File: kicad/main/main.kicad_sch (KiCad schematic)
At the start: 52 parts, among them J1 to cam, J10 I2C_1, J11 drib-kick, J12 drib-kick, J14 5V OUT, J15 LINE, J3 USB_C_Receptacle_USB2.0, J4 Power IN, J5 MD1, J6 MD2, J7 Serial0/XBee, J8 Serial1/IMU, J9 AUX1, Q1 AO3400A, Q2 AO3401A, SW1 BTN_UP, SW2 BTN_UP, SW3 Reset, U2 RP2040_Stamp, U3 74HC32, U4 74HC04, U5 OKL-T_3-W12N-C

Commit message: main bus
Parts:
- J2: value (none) -> I2C_2; footprint (none) -> 0.main.robot:JSTB4B-ZR
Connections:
- net +5V: no longer J8.2 (Pin_2)
- net GND: now also SW?.1; no longer J8.4 (Pin_4)
- net SW1_5: no longer U2.8 (GPIO7)
- net IMU SET: now reaches SW?.2
- net IMU SET: now also U2.24 (GPIO23)
- net SCL_I2C0 renamed I2C_0.SCL
- net SCL_I2C1 renamed I2C_1.SCL
- net SDA_I2C0 renamed I2C_0.SDA
- net SDA_I2C1 renamed I2C_1.SDA
- net USB_D+ renamed USB.D+
- net USB_D- renamed USB.D-
- new net: J8.4 (Pin_4), U2.8 (GPIO7)
- no-connect marks 11 -> 14
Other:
- moved on the sheet: SW?

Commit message: update
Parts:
- gave numbers to parts that had none: 1
- renumbered C3 to C1, C4 to C2, C5 to C3, C6 to C4, D3 to D1, D4 to D2, D1 to D3, D5 to D4, D6 to D5, J3 to J1, J14 to J13, J15 to J14, J4 to J3, J5 to J4, J6 to J5, J7 to J6, J8 to J7, J9 to J8, J1 to J9, R3 to R1, R11 to R10, R12 to R11, R13 to R12, R14 to R13, R15 to R14, R16 to R15, R17 to R16, R18 to R17, R19 to R18, R20 to R19, R4 to R2, R1 to R3, R5 to R4, R6 to R5, R7 to R6, R8 to R7, R9 to R8, R10 to R9, SW3 to SW4, U2 to U1, U3 to U2, U4 to U3, U5 to U4

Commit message: update: main
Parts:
- removed J8: AUX1, 0.main.robot:JSTB4B-ZR, symbol Connector_Generic:Conn_01x04
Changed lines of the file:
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@@
     (stroke (width 0) (type solid) (color 0 0 0 0))
   )
-  (wire (pts (xy 226.06 163.83) (xy 236.22 163.83))
-    (stroke (width 0) (type default) (color 0 0 0 0))
-  )
   (wire (pts (xy 294.64 245.11) (xy 328.93 245.11))
     (stroke (width 0) (type default) (color 0 0 0 0))
@@
     (stroke (width 0) (type default) (color 0 0 0 0))
   )
-  (wire (pts (xy 226.06 168.91) (xy 226.06 163.83))
-    (stroke (width 0) (type default) (color 0 0 0 0))
-  )
   (wire (pts (xy 346.71 109.22) (xy 345.44 109.22))
     (stroke (width 0) (type default) (color 0 0 0 0))
@@
     (stroke (width 0) (type default) (color 0 0 0 0))
   )
-  (wire (pts (xy 236.22 161.29) (xy 223.52 161.29))
-    (stroke (width 0) (type default) (color 0 0 0 0))
-  )
   (wire (pts (xy 339.09 22.86) (xy 339.09 29.21))
     (stroke (width 0) (type default) (color 0 0 0 0))
@@
     (stroke (width 0) (type default) (color 0 0 0 0))
   )
-  (wire (pts (xy 228.6 168.91) (xy 228.6 166.37))
-    (stroke (width 0) (type default) (color 0 0 0 0))
-  )
   (wire (pts (xy 166.37 27.94) (xy 166.37 33.02))
     (stroke (width 0) (type default) (color 0 0 0 0))
@@
     (stroke (width 0) (type default) (color 0 0 0 0))
   )
-  (wire (pts (xy 175.26 168.91) (xy 226.06 168.91))
-    (stroke (width 0) (type default) (color 0 0 0 0))
-  )
   (wire (pts (xy 312.42 41.91) (xy 314.96 41.91))
     (stroke (width 0) (type default) (color 0 0 0 0))
   )
-  (wire (pts (xy 223.52 161.29) (xy 223.52 158.75))
-    (stroke (width 0) (type default) (color 0 0 0 0))
-  )
   (wire (pts (xy 322.58 46.99) (xy 325.12 46.99))
     (stroke (width 0) (type default) (color 0 0 0 0))
@@
     (stroke (width 0) (type solid) (color 0 0 0 0))
   )
-  (wire (pts (xy 236.22 168.91) (xy 228.6 168.91))
-    (stroke (width 0) (type default) (color 0 0 0 0))
-  )
   (wire (pts (xy 177.8 204.47) (xy 175.26 204.47))
     (stroke (width 0) (type default) (color 0 0 0 0))
@@
     (stroke (width 0) (type default) (color 0 0 0 0))
   )
-  (wire (pts (xy 236.22 166.37) (xy 231.14 166.37))
-    (stroke (width 0) (type default) (color 0 0 0 0))
-  )
   (wire (pts (xy 213.36 109.22) (xy 218.44 109.22))
     (stroke (width 0) (type default) (color 0 0 0 0))
@@
     (stroke (width 0) (type default) (color 0 0 0 0))
   )
-  (wire (pts (xy 231.14 166.37) (xy 231.14 172.72))
-    (stroke (width 0) (type default) (color 0 0 0 0))
-  )
   (wire (pts (xy 302.26 170.18) (xy 302.26 171.45))
     (stroke (width 0) (type default) (color 0 0 0 0))
@@
     (stroke (width 0) (type solid) (color 0 0 0 0))
   )
-  (wire (pts (xy 228.6 166.37) (xy 175.26 166.37))
-    (stroke (width 0) (type default) (color 0 0 0 0))
-  )
   (wire (pts (xy 259.08 71.12) (xy 259.08 66.04))
     (stroke (width 0) (type default) (color 0 0 0 0))
@@
     (pin "2")
   )
-  (symbol (lib_id "power:GND") (at 223.52 158.75 180) (unit 1)
-    (in_bom yes) (on_board yes)
-    (property "Reference" "#PWR019" (id 0) (at 223.52 152.4 0)
-      (effects (font (size 1.27 1.27)) hide)
-    )
-    (property "Value" "GND" (id 1) (at 223.393 154.3558 0))
-    (property "Footprint" "" (id 2) (at 223.52 158.75 0)
-      (effects (font (size 1.27 1.27)) hide)
-    )
-    (property "Datasheet" "" (id 3) (at 223.52 158.75 0)
-      (effects (font (size 1.27 1.27)) hide)
-    )
-    (pin "1")
-  )
-  (symbol (lib_id "power:+3V3") (at 231.14 172.72 180) (unit 1)
-    (in_bom yes) (on_board yes)
-    (property "Reference" "#PWR020" (id 0) (at 231.14 168.91 0)
-      (effects (font (size 1.27 1.27)) hide)
-    )
-    (property "Value" "+3V3" (id 1) (at 230.759 177.1142 0))
-    (property "Footprint" "" (id 2) (at 231.14 172.72 0)
-      (effects (font (size 1.27 1.27)) hide)
-    )
-    (property "Datasheet" "" (id 3) (at 231.14 172.72 0)
-      (effects (font (size 1.27 1.27)) hide)
-    )
-    (pin "1")
-  )
   (symbol (lib_id "Device:R_Small") (at 58.42 33.02 90) (unit 1)
     (in_bom yes) (on_board yes)
@@
     (pin "4")
   )
-  (symbol (lib_id "Connector_Generic:Conn_01x04") (at 241.3 166.37 0) (mirror x) (unit 1)
-    (in_bom yes) (on_board yes)
-    (property "Reference" "J8" (id 0) (at 239.2172 174.4218 0))
-    (property "Value" "AUX1" (id 1) (at 239.2172 172.1104 0))
-    (property "Footprint" "0.main.robot:JSTB4B-ZR" (id 2) (at 241.3 166.37 0)
-      (effects (font (size 1.27 1.27)) hide)
-    )
-    (property "Datasheet" "~" (id 3) (at 241.3 166.37 0)
-      (effects (font (size 1.27 1.27)) hide)
-    )
-    (pin "1")
-    (pin "2")
-    (pin "3")
-    (pin "4")
-  )
   (symbol (lib_id "power:PWR_FLAG") (at 393.7 86.36 180) (unit 1)
     (in_bom yes) (on_board yes)
@@
       (reference "#PWR018") (unit 1) (value "GND") (footprint "")
     )
-    (path "/752fc55c-e76e-432a-bc83-693481fcb78d"
-      (reference "#PWR019") (unit 1) (value "GND") (footprint "")
-    )
-    (path "/77d14d57-9085-4f50-abb6-179e39dad366"
-      (reference "#PWR020") (unit 1) (value "+3V3") (footprint "")
-    )
     (path "/9fd19139-adbc-41aa-8bcf-e1f4d9d99653"
       (reference "#PWR021") (unit 1) (value "GND") (footprint "")
@@
       (reference "J7") (unit 1) (value "Serial1/IMU") (footprint "0.main.robot:JSTB4B-ZR")
     )
-    (path "/a1be515e-a7bb-43c1-b1bb-0aba8f0efd17"
-      (reference "J8") (unit 1) (value "AUX1") (footprint "0.main.robot:JSTB4B-ZR")
-    )
     (path "/05c35a87-473b-4928-9233-cb895723bf3b"
       (reference "J9") (unit 1) (value "to cam") (footprint "0.main.robot:JSTB6B-ZR")
@@
     )
     (path "/17adc8c0-c792-4780-aab1-71d31733c779/2f24ee3a-bda6-4bf4-babd-453edbada110"
-      (reference "R22") (unit 1) (value "47k") (footprint "Resistor_SMD:R_0603_1608Metric_Pad0.98x0.95mm_HandSolder")
+      (reference "R22") (unit 1) (value "10k") (footprint "Resistor_SMD:R_0603_1608Metric_Pad0.98x0.95mm_HandSolder")
     )
     (path "/17adc8c0-c792-4780-aab1-71d31733c779/7df5ac02-e953-460c-b9a0-008c0199109a"
-      (reference "R23") (unit 1) (value "47k") (footprint "Resistor_SMD:R_0603_1608Metric_Pad0.98x0.95mm_HandSolder")
+      (reference "R23") (unit 1) (value "10k") (footprint "Resistor_SMD:R_0603_1608Metric_Pad0.98x0.95mm_HandSolder")
     )
     (path "/17adc8c0-c792-4780-aab1-71d31733c779/84fcf317-1dbc-4fc4-ae20-4a2661c3f9e2"
@@
     )
     (path "/54dc5971-37b9-46a7-8049-349fe99f9b14/d76ca0c0-136b-45bb-a75a-1d5f857a267b"
-      (reference "R27") (unit 1) (value "47k") (footprint "Resistor_SMD:R_0603_1608Metric_Pad0.98x0.95mm_HandSolder")
+      (reference "R27") (unit 1) (value "10k") (footprint "Resistor_SMD:R_0603_1608Metric_Pad0.98x0.95mm_HandSolder")
     )
     (path "/54dc5971-37b9-46a7-8049-349fe99f9b14/30999beb-a697-4427-87eb-804dc1f57005"
-      (reference "R28") (unit 1) (value "47k") (footprint "Resistor_SMD:R_0603_1608Metric_Pad0.98x0.95mm_HandSolder")
+      (reference "R28") (unit 1) (value "10k") (footprint "Resistor_SMD:R_0603_1608Metric_Pad0.98x0.95mm_HandSolder")
     )
     (path "/54dc5971-37b9-46a7-8049-349fe99f9b14/35102534-5042-4dae-ac97-e5de032ae706"

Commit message: SW-LED changed
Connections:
- net SW1_2: now also U1.15 (GPIO14); no longer U1.7 (GPIO6)
- net SW1_5: now also U1.16 (GPIO15)
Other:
- note added: "SW-G"
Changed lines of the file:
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@@
   (no_connect (at 177.8 204.47))
   (no_connect (at 279.4 39.37))
+  (no_connect (at 175.26 146.05))
   (no_connect (at 279.4 41.91))
   (no_connect (at 203.2 196.85))
   (no_connect (at 52.07 53.34))
-  (no_connect (at 243.84 104.14))
   (no_connect (at 52.07 55.88))
   (no_connect (at 203.2 194.31))
@@
     (stroke (width 0) (type default) (color 0 0 0 0))
   )
+  (wire (pts (xy 199.39 168.91) (xy 175.26 168.91))
+    (stroke (width 0) (type default) (color 0 0 0 0))
+  )
   (wire (pts (xy 175.26 151.13) (xy 207.01 151.13))
     (stroke (width 0) (type default) (color 0 0 0 0))
@@
     (stroke (width 0) (type default) (color 0 0 0 0))
   )
-  (wire (pts (xy 175.26 146.05) (xy 196.85 146.05))
-    (stroke (width 0) (type default) (color 0 0 0 0))
-  )
   (wire (pts (xy 60.96 33.02) (xy 67.31 33.02))
     (stroke (width 0) (type solid) (color 0 0 0 0))
@@
     (stroke (width 0) (type default) (color 0 0 0 0))
   )
-  (wire (pts (xy 196.85 146.05) (xy 196.85 96.52))
-    (stroke (width 0) (type default) (color 0 0 0 0))
-  )
   (wire (pts (xy 175.26 135.89) (xy 191.77 135.89))
     (stroke (width 0) (type default) (color 0 0 0 0))
@@
     (stroke (width 0) (type default) (color 0 0 0 0))
   )
+  (wire (pts (xy 199.39 104.14) (xy 260.35 104.14))
+    (stroke (width 0) (type default) (color 0 0 0 0))
+  )
   (wire (pts (xy 52.07 43.18) (xy 53.34 43.18))
     (stroke (width 0) (type solid) (color 0 0 0 0))
@@
     (stroke (width 0) (type default) (color 0 0 0 0))
   )
-  (wire (pts (xy 260.35 104.14) (xy 243.84 104.14))
+  (wire (pts (xy 196.85 96.52) (xy 196.85 166.37))
     (stroke (width 0) (type default) (color 0 0 0 0))
   )
@@
     (stroke (width 0) (type default) (color 0 0 0 0))
   )
+  (wire (pts (xy 199.39 104.14) (xy 199.39 168.91))
+    (stroke (width 0) (type default) (color 0 0 0 0))
+  )
   (wire (pts (xy 260.35 99.06) (xy 254 99.06))
     (stroke (width 0) (type default) (color 0 0 0 0))
@@
     (stroke (width 0) (type default) (color 0 0 0 0))
   )
+  (wire (pts (xy 196.85 166.37) (xy 175.26 166.37))
+    (stroke (width 0) (type default) (color 0 0 0 0))
+  )
   (wire (pts (xy 323.85 195.58) (xy 323.85 217.17))
     (stroke (width 0) (type default) (color 0 0 0 0))
@@
     (effects (font (size 1.27 1.27) (thickness 0.254) bold italic) (justify left bottom))
   )
+  (text "SW-G" (at 254 104.14 0)
+    (effects (font (size 1.27 1.27) (thickness 0.254) bold italic) (justify left bottom))
+  )
   (text "SW-R" (at 254 96.52 0)
     (effects (font (size 1.27 1.27) (thickness 0.254) bold italic) (justify left bottom))
@@
     )
     (path "/70fde810-700d-485a-8c97-2da167292bf1/00000000-0000-0000-0000-00005f414703"
-      (reference "R31") (unit 1) (value "470") (footprint "Resistor_SMD:R_0603_1608Metric_Pad0.98x0.95mm_HandSolder")
+      (reference "R31") (unit 1) (value "120") (footprint "Resistor_SMD:R_0603_1608Metric_Pad0.98x0.95mm_HandSolder")
     )
     (path "/70fde810-700d-485a-8c97-2da167292bf1/00000000-0000-0000-0000-00005fd99a16"
@@
     )
     (path "/70fde810-700d-485a-8c97-2da167292bf1/00000000-0000-0000-0000-00005f414122"
-      (reference "R34") (unit 1) (value "470") (footprint "Resistor_SMD:R_0603_1608Metric_Pad0.98x0.95mm_HandSolder")
+      (reference "R34") (unit 1) (value "120") (footprint "Resistor_SMD:R_0603_1608Metric_Pad0.98x0.95mm_HandSolder")
     )
     (path "/70fde810-700d-485a-8c97-2da167292bf1/81b32344-4ecf-4492-a65b-88cfe75f389e"

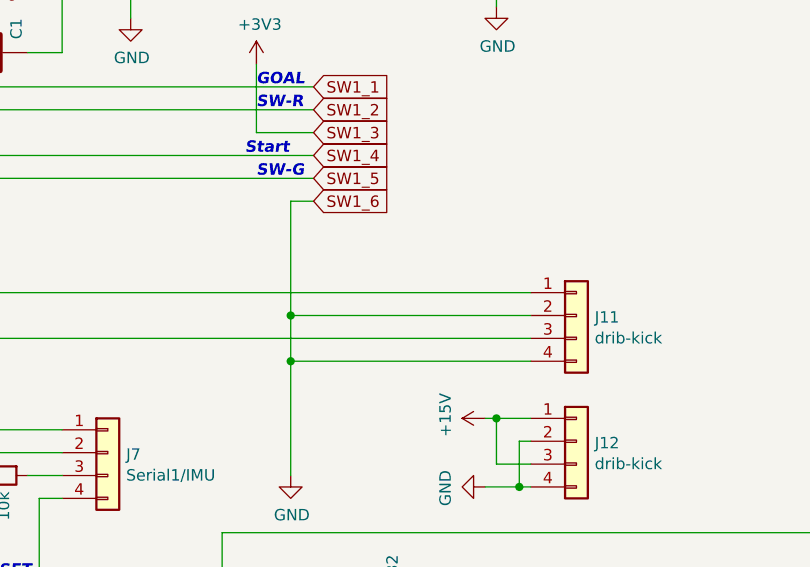
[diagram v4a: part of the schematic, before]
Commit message: KickerのGND変更
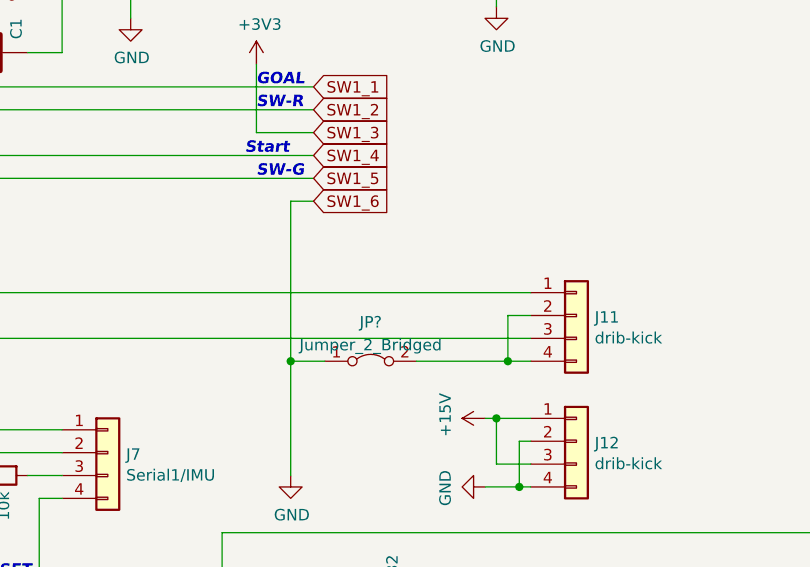
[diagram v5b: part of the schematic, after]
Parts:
- added JP?: Jumper_2_Bridged, symbol Jumper:Jumper_2_Bridged
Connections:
- net GND: now also JP?.1 (A); no longer J11.2 (Pin_2), J11.4 (Pin_4)
- new net: J11.2 (Pin_2), J11.4 (Pin_4), JP?.2 (B)
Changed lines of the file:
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@@
   (junction (at 76.2 128.27) (diameter 0) (color 0 0 0 0)
   )
+  (junction (at 281.94 124.46) (diameter 0) (color 0 0 0 0)
+  )
   (junction (at 218.44 52.07) (diameter 0) (color 0 0 0 0)
   )
@@
   (junction (at 241.3 52.07) (diameter 0) (color 0 0 0 0)
   )
-  (junction (at 257.81 119.38) (diameter 0) (color 0 0 0 0)
-  )
   (junction (at 53.34 43.18) (diameter 1.016) (color 0 0 0 0)
   )
@@
     (stroke (width 0) (type default) (color 0 0 0 0))
   )
-  (wire (pts (xy 257.81 119.38) (xy 257.81 124.46))
+  (wire (pts (xy 257.81 106.68) (xy 257.81 124.46))
     (stroke (width 0) (type default) (color 0 0 0 0))
   )
@@
     (stroke (width 0) (type default) (color 0 0 0 0))
   )
-  (wire (pts (xy 257.81 119.38) (xy 284.48 119.38))
-    (stroke (width 0) (type default) (color 0 0 0 0))
-  )
   (wire (pts (xy 175.26 133.35) (xy 186.69 133.35))
     (stroke (width 0) (type default) (color 0 0 0 0))
@@
     (stroke (width 0) (type solid) (color 0 0 0 0))
   )
+  (wire (pts (xy 281.94 124.46) (xy 271.78 124.46))
+    (stroke (width 0) (type default) (color 0 0 0 0))
+  )
   (wire (pts (xy 392.43 208.28) (xy 358.14 208.28))
     (stroke (width 0) (type default) (color 0 0 0 0))
@@
     (stroke (width 0) (type default) (color 0 0 0 0))
   )
-  (wire (pts (xy 257.81 106.68) (xy 257.81 119.38))
-    (stroke (width 0) (type default) (color 0 0 0 0))
-  )
   (wire (pts (xy 358.14 208.28) (xy 358.14 215.9))
     (stroke (width 0) (type default) (color 0 0 0 0))
@@
     (stroke (width 0) (type default) (color 0 0 0 0))
   )
-  (wire (pts (xy 284.48 124.46) (xy 257.81 124.46))
+  (wire (pts (xy 284.48 124.46) (xy 281.94 124.46))
     (stroke (width 0) (type default) (color 0 0 0 0))
   )
@@
     (stroke (width 0) (type default) (color 0 0 0 0))
   )
+  (wire (pts (xy 261.62 124.46) (xy 257.81 124.46))
+    (stroke (width 0) (type default) (color 0 0 0 0))
+  )
   (wire (pts (xy 210.82 63.5) (xy 210.82 90.17))
     (stroke (width 0) (type default) (color 0 0 0 0))
@@
     (stroke (width 0) (type default) (color 0 0 0 0))
   )
+  (wire (pts (xy 284.48 119.38) (xy 281.94 119.38))
+    (stroke (width 0) (type default) (color 0 0 0 0))
+  )
   (wire (pts (xy 279.4 130.81) (xy 280.67 130.81))
     (stroke (width 0) (type default) (color 0 0 0 0))
@@
     (stroke (width 0) (type default) (color 0 0 0 0))
   )
+  (wire (pts (xy 281.94 119.38) (xy 281.94 124.46))
+    (stroke (width 0) (type default) (color 0 0 0 0))
+  )
   (wire (pts (xy 326.39 29.21) (xy 339.09 29.21))
     (stroke (width 0) (type default) (color 0 0 0 0))
@@
     (pin "1")
   )
+  (symbol (lib_id "Jumper:Jumper_2_Bridged") (at 266.7 124.46 0) (unit 1)
+    (in_bom yes) (on_board yes) (fields_autoplaced)
+    (property "Reference" "JP?" (id 0) (at 266.7 120.1252 0))
+    (property "Value" "Jumper_2_Bridged" (id 1) (at 266.7 122.6621 0))
+    (property "Footprint" "" (id 2) (at 266.7 124.46 0)
+      (effects (font (size 1.27 1.27)) hide)
+    )
+    (property "Datasheet" "~" (id 3) (at 266.7 124.46 0)
+      (effects (font (size 1.27 1.27)) hide)
+    )
+    (pin "1")
+    (pin "2")
+  )
   (symbol (lib_id "Connector_Generic:Conn_01x02") (at 153.67 22.86 270) (mirror x) (unit 1)
     (in_bom yes) (on_board yes)
@@
       (reference "JP1") (unit 1) (value "Jumper_2_Bridged") (footprint "Connector_PinHeader_1.27mm:PinHeader_1x02_P1.27mm_Vertical")
     )
+    (path "/8f35d220-c53a-42e9-9bdd-e2fe7cb741d3"
+      (reference "JP?") (unit 1) (value "Jumper_2_Bridged") (footprint "")
+    )
     (path "/550b4c3d-d7ae-47ac-897c-516108b07dc8"
